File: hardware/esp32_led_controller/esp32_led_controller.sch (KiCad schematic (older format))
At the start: 47 parts, among them J1 USB_B, J2 CONN_01X09, J3 CONN_01X08, J4 BARREL_JACK, J5 CONN_01X03, J6 USB_C_Receptacle_USB2.0, Q1 Q_NPN_BEC, Q2 Q_NPN_BEC, SW1 SW_Push, U1 MCP1415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

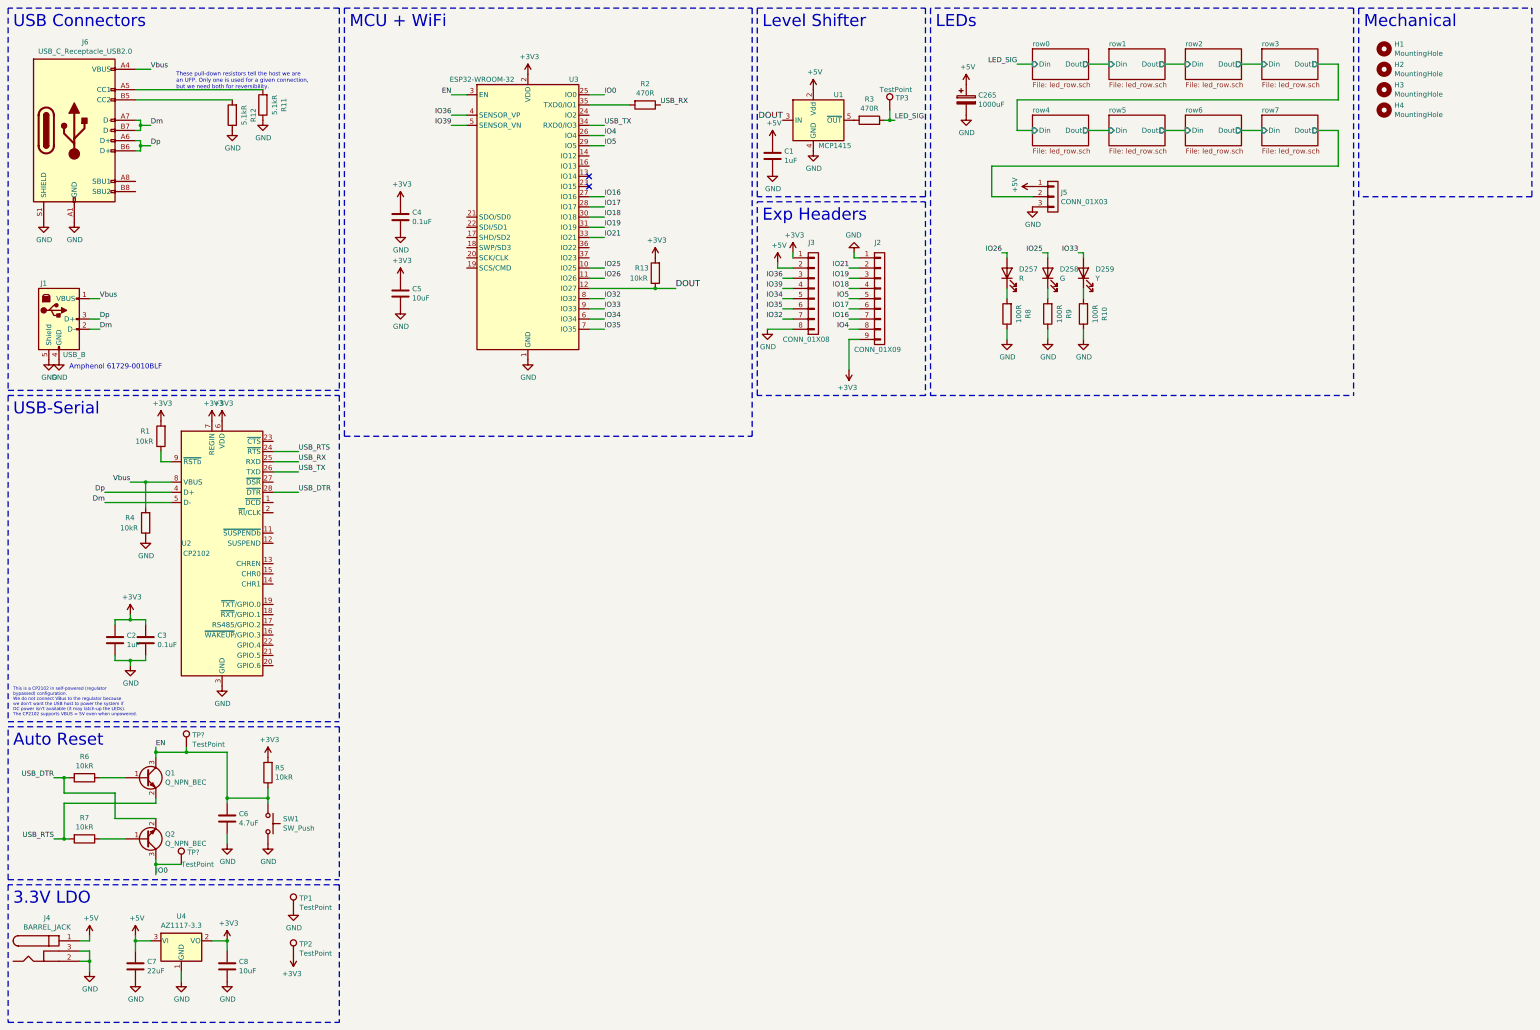
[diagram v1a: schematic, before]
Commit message: Added configuration jumpers
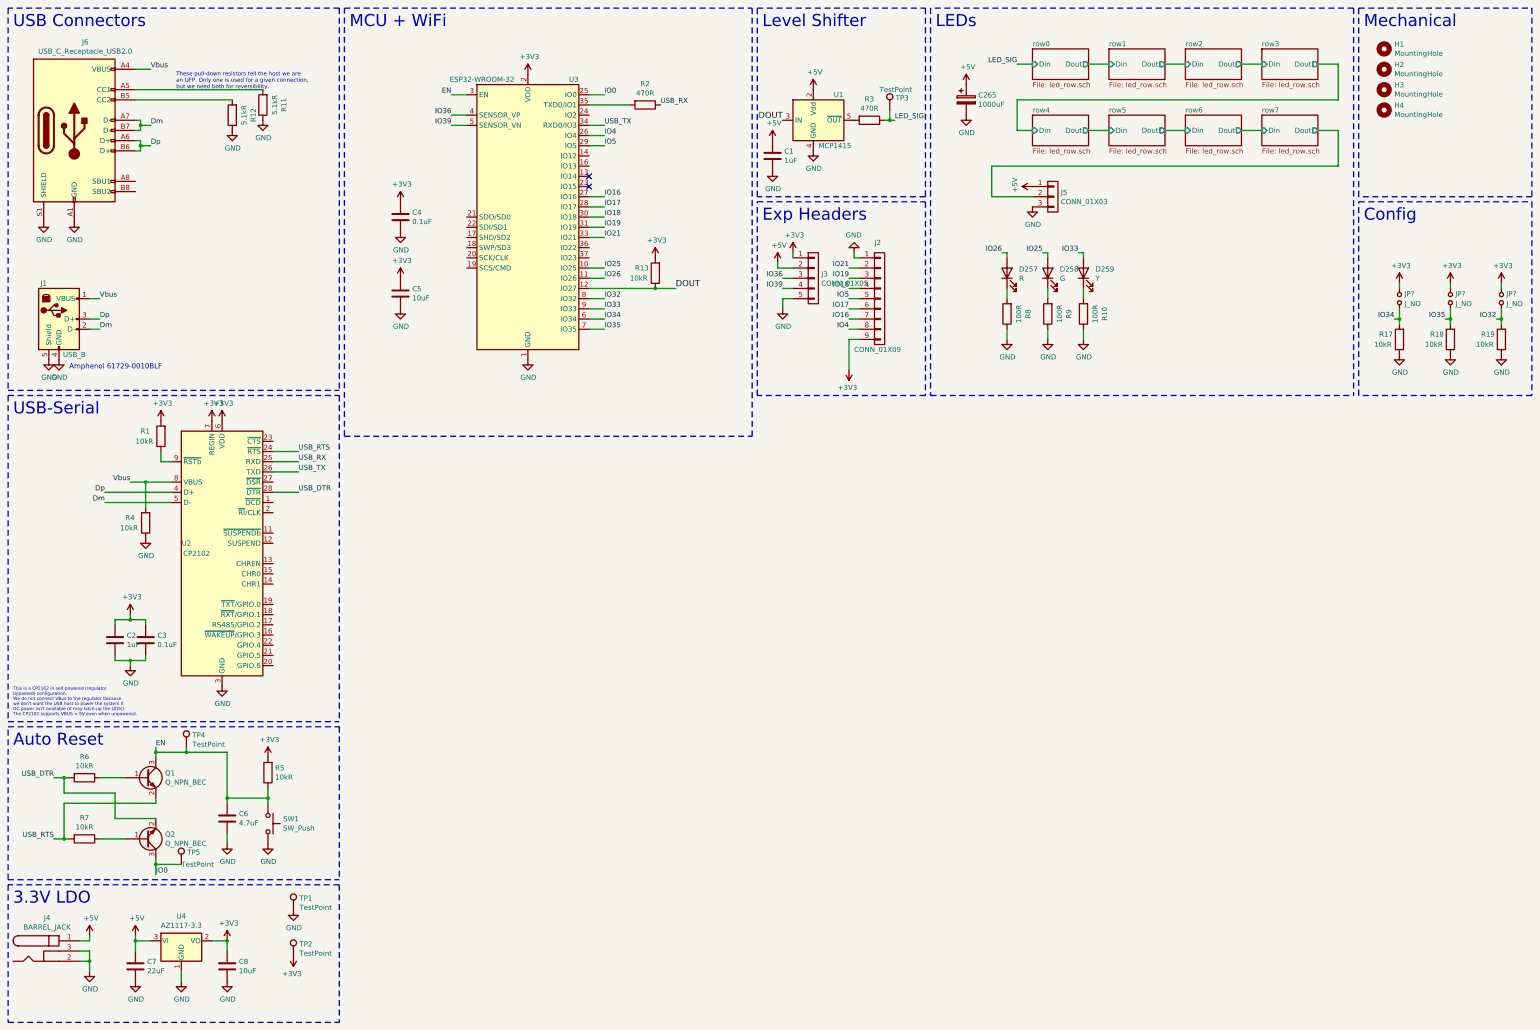
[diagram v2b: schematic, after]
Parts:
- removed J3: CONN_01X08, Connector_PinHeader_2.54mm:PinHeader_1x08_P2.54mm_Vertical, symbol conn:CONN_01X08
- added J3: CONN_01X05, Connector_PinHeader_2.54mm:PinHeader_1x05_P2.54mm_Vertical, symbol conn:CONN_01X05
- added JP? (x3): J_NO, Jumper:SolderJumper-2_P1.3mm_Open_TrianglePad1.0x1.5mm, symbol Device:Jumper_NO_Small
- added R17, R18, R19: 10kR, Resistor_SMD:R_0402_1005Metric, symbol Device:R
- gave numbers to parts that had none: 2
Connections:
- net +3V3: now also J3.1 (P1), JP?.1, JP?.1, JP?.1
- net +5V: now also J3.2 (P2)
- net GND: now also J3.5 (P5), R17.1, R18.1, R19.1
- net IO32: now also JP?.2, R19.2
- net IO34: now also JP?.2, R17.2
- net IO35: now also JP?.2, R18.2
- net IO36: now also J3.3 (P3)
- net IO39: now also J3.4 (P4)
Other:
- note added: "Config"
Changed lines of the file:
@@
 Wire Wire Line
 	6550 4100 6700 4100
-Text Label 8450 3800 2    50   ~ 0
+Text Label 14450 4000 2    50   ~ 0
 IO34
-Text Label 8450 3900 2    50   ~ 0
-IO35
 Text Label 6700 3900 0    50   ~ 0
 IO33
@@
 Wire Wire Line
 	6550 3900 6700 3900
-Text Label 8450 4000 2    50   ~ 0
-IO32
 Text Label 11350 3350 2    50   ~ 0
 IO33
@@
 	1    0    0    -1
 $EndComp
-Wire Wire Line
-	8450 4000 8550 4000
-Wire Wire Line
-	8550 3900 8450 3900
-Wire Wire Line
-	8550 3800 8450 3800
 Wire Wire Line
 	8450 3700 8550 3700
@@
 L power:GND #PWR?
 U 1 1 605F1340
-P 8300 4100
+P 8450 3900
 AR Path="/5F1ED570/605F1340" Ref="#PWR?"  Part="1"
 AR Path="/605F1340" Ref="#PWR01060"  Part="1"
-F 0 "#PWR01060" H 8300 3850 50  0001 C CNN
-F 1 "GND" H 8305 3927 50  0000 C CNN
-F 2 "" H 8300 4100 50  0001 C CNN
-F 3 "" H 8300 4100 50  0001 C CNN
-	1    8300 4100
+F 0 "#PWR01060" H 8450 3650 50  0001 C CNN
+F 1 "GND" H 8455 3727 50  0000 C CNN
+F 2 "" H 8450 3900 50  0001 C CNN
+F 3 "" H 8450 3900 50  0001 C CNN
+	1    8450 3900
 	1    0    0    -1
 $EndComp
@@
 Wire Wire Line
 	8400 3500 8550 3500
-Wire Wire Line
-	8300 4100 8550 4100
-$Comp
-L conn:CONN_01X08 J3
-U 1 1 606C16D0
-P 8750 3750
-F 0 "J3" H 8700 4250 50  0000 L CNN
-F 1 "CONN_01X08" H 8450 3300 50  0000 L CNN
-F 2 "Connector_PinHeader_2.54mm:PinHeader_1x08_P2.54mm_Vertical" H 8750 3750 50  0001 C CNN
-F 3 "" H 8750 3750 50  0001 C CNN
-	1    8750 3750
-	1    0    0    -1
-$EndComp
 $Comp
 L Device:LED D257
@@
 $EndComp
 $Comp
-L Connector:TestPoint TP?
+L Connector:TestPoint TP4
 U 1 1 6025CD38
 P 2600 8200
-F 0 "TP?" H 2658 8318 50  0000 L CNN
+F 0 "TP4" H 2658 8318 50  0000 L CNN
 F 1 "TestPoint" H 2658 8227 50  0000 L CNN
 F 2 "TestPoint:TestPoint_Loop_D3.50mm_Drill1.4mm_Beaded" H 2800 8200 50  0001 C CNN
@@
 $EndComp
 $Comp
-L Connector:TestPoint TP?
+L Connector:TestPoint TP5
 U 1 1 6025DADF
 P 2550 9350
-F 0 "TP?" H 2608 9468 50  0000 L CNN
+F 0 "TP5" H 2608 9468 50  0000 L CNN
 F 1 "TestPoint" H 2550 9350 50  0000 L CNN
 F 2 "TestPoint:TestPoint_Loop_D3.50mm_Drill1.4mm_Beaded" H 2750 9350 50  0001 C CNN
@@
 Wire Wire Line
 	2600 8250 3000 8250
+Wire Notes Line
+	14100 2850 15800 2850
+Wire Notes Line
+	15800 2850 15800 4750
+Wire Notes Line
+	15800 4750 14100 4750
+Wire Notes Line
+	14100 4750 14100 2850
+Text Notes 14150 3050 0    118  ~ 0
+Config
+$Comp
+L Device:R R?
+U 1 1 6028F8B2
+P 14500 4200
+AR Path="/5F1ED570/6028F8B2" Ref="R?"  Part="1"
+AR Path="/6028F8B2" Ref="R17"  Part="1"
+F 0 "R17" H 14700 4150 50  0000 R CNN
+F 1 "10kR" H 14750 4250 50  0000 R CNN
+F 2 "Resistor_SMD:R_0402_1005Metric" V 14430 4200 50  0001 C CNN
+F 3 "~" H 14500 4200 50  0001 C CNN
+F 4 "C25744" V 14500 4200 50  0001 C CNN "LCSC"
+	1    14500 4200
+	-1   0    0    1
+$EndComp
+$Comp
+L Device:R R?
+U 1 1 60290F37
+P 15000 4200
+AR Path="/5F1ED570/60290F37" Ref="R?"  Part="1"
+AR Path="/60290F37" Ref="R18"  Part="1"
+F 0 "R18" H 15200 4150 50  0000 R CNN
+F 1 "10kR" H 15250 4250 50  0000 R CNN
+F 2 "Resistor_SMD:R_0402_1005Metric" V 14930 4200 50  0001 C CNN
+F 3 "~" H 15000 4200 50  0001 C CNN
+F 4 "C25744" V 15000 4200 50  0001 C CNN "LCSC"
+	1    15000 4200
+	-1   0    0    1
+$EndComp
+$Comp
+L Device:R R?
+U 1 1 6029126C
+P 15500 4200
+AR Path="/5F1ED570/6029126C" Ref="R?"  Part="1"
+AR Path="/6029126C" Ref="R19"  Part="1"
+F 0 "R19" H 15700 4150 50  0000 R CNN
+F 1 "10kR" H 15750 4250 50  0000 R CNN
+F 2 "Resistor_SMD:R_0402_1005Metric" V 15430 4200 50  0001 C CNN
+F 3 "~" H 15500 4200 50  0001 C CNN
+F 4 "C25744" V 15500 4200 50  0001 C CNN "LCSC"
+	1    15500 4200
+	-1   0    0    1
+$EndComp
+$Comp
+L power:+3V3 #PWR?
+U 1 1 6029175F
+P 14500 3650
+AR Path="/5F1ED570/6029175F" Ref="#PWR?"  Part="1"
+AR Path="/6029175F" Ref="#PWR01074"  Part="1"
+F 0 "#PWR01074" H 14500 3500 50  0001 C CNN
+F 1 "+3V3" H 14515 3823 50  0000 C CNN
+F 2 "" H 14500 3650 50  0001 C CNN
+F 3 "" H 14500 3650 50  0001 C CNN
+	1    14500 3650
+	1    0    0    -1
+$EndComp
+$Comp
+L power:+3V3 #PWR?
+U 1 1 60291FEB
+P 15000 3650
+AR Path="/5F1ED570/60291FEB" Ref="#PWR?"  Part="1"
+AR Path="/60291FEB" Ref="#PWR01075"  Part="1"
+F 0 "#PWR01075" H 15000 3500 50  0001 C CNN
+F 1 "+3V3" H 15015 3823 50  0000 C CNN
+F 2 "" H 15000 3650 50  0001 C CNN
+F 3 "" H 15000 3650 50  0001 C CNN
+	1    15000 3650
+	1    0    0    -1
+$EndComp
+$Comp
+L power:+3V3 #PWR?
+U 1 1 6029236B
+P 15500 3650
+AR Path="/5F1ED570/6029236B" Ref="#PWR?"  Part="1"
+AR Path="/6029236B" Ref="#PWR01076"  Part="1"
+F 0 "#PWR01076" H 15500 3500 50  0001 C CNN
+F 1 "+3V3" H 15515 3823 50  0000 C CNN
+F 2 "" H 15500 3650 50  0001 C CNN
+F 3 "" H 15500 3650 50  0001 C CNN
+	1    15500 3650
+	1    0    0    -1
+$EndComp
+$Comp
+L power:GND #PWR?
+U 1 1 60299D69
+P 14500 4350
+AR Path="/5F1ED570/60299D69" Ref="#PWR?"  Part="1"
+AR Path="/60299D69" Ref="#PWR01077"  Part="1"
+F 0 "#PWR01077" H 14500 4100 50  0001 C CNN
+F 1 "GND" H 14505 4177 50  0000 C CNN
+F 2 "" H 14500 4350 50  0001 C CNN
+F 3 "" H 14500 4350 50  0001 C CNN
+	1    14500 4350
+	1    0    0    -1
+$EndComp
+$Comp
+L power:GND #PWR?
+U 1 1 6029A13A
+P 15000 4350
+AR Path="/5F1ED570/6029A13A" Ref="#PWR?"  Part="1"
+AR Path="/6029A13A" Ref="#PWR01078"  Part="1"
+F 0 "#PWR01078" H 15000 4100 50  0001 C CNN
+F 1 "GND" H 15005 4177 50  0000 C CNN
+F 2 "" H 15000 4350 50  0001 C CNN
+F 3 "" H 15000 4350 50  0001 C CNN
+	1    15000 4350
+	1    0    0    -1
+$EndComp
+$Comp
+L power:GND #PWR?
+U 1 1 6029A31F
+P 15500 4350
+AR Path="/5F1ED570/6029A31F" Ref="#PWR?"  Part="1"
+AR Path="/6029A31F" Ref="#PWR01079"  Part="1"
+F 0 "#PWR01079" H 15500 4100 50  0001 C CNN
+F 1 "GND" H 15505 4177 50  0000 C CNN
+F 2 "" H 15500 4350 50  0001 C CNN
+F 3 "" H 15500 4350 50  0001 C CNN
+	1    15500 4350
+	1    0    0    -1
+$EndComp
+Wire Wire Line
+	14450 4000 14500 4000
+Wire Wire Line
+	14500 4000 14500 4050
+Connection ~ 14500 4000
+Text Label 14950 4000 2    50   ~ 0
+IO35
+Text Label 15450 4000 2    50   ~ 0
+IO32
+$Comp
+L conn:CONN_01X05 J3
+U 1 1 602A9206
+P 8750 3600
+F 0 "J3" H 8828 3641 50  0000 L CNN
+F 1 "CONN_01X05" H 8828 3550 50  0000 L CNN
+F 2 "Connector_PinHeader_2.54mm:PinHeader_1x05_P2.54mm_Vertical" H 8750 3600 50  0001 C CNN
+F 3 "" H 8750 3600 50  0001 C CNN
+	1    8750 3600
+	1    0    0    -1
+$EndComp
+Wire Wire Line
+	8450 3900 8450 3800
+Wire Wire Line
+	8450 3800 8550 3800
+Wire Wire Line
+	14950 4000 15000 4000
+Connection ~ 15000 4000
+Wire Wire Line
+	15000 4000 15000 4050
+Wire Wire Line
+	15450 4000 15500 4000
+Connection ~ 15500 4000
+Wire Wire Line
+	15500 4000 15500 4050
+$Comp
+L Device:Jumper_NO_Small JP?
+U 1 1 60328712
+P 15000 3800
+F 0 "JP?" V 14954 3848 50  0000 L CNN
+F 1 "J_NO" V 15050 3850 50  0000 L CNN
+F 2 "Jumper:SolderJumper-2_P1.3mm_Open_TrianglePad1.0x1.5mm" H 15000 3800 50  0001 C CNN
+F 3 "~" H 15000 3800 50  0001 C CNN
+	1    15000 3800
+	0    1    1    0
+$EndComp
+$Comp
+L Device:Jumper_NO_Small JP?
+U 1 1 60329C4C
+P 14500 3800
+F 0 "JP?" V 14454 3848 50  0000 L CNN
+F 1 "J_NO" V 14550 3850 50  0000 L CNN
+F 2 "Jumper:SolderJumper-2_P1.3mm_Open_TrianglePad1.0x1.5mm" H 14500 3800 50  0001 C CNN
+F 3 "~" H 14500 3800 50  0001 C CNN
+	1    14500 3800
+	0    1    1    0
+$EndComp
+$Comp
+L Device:Jumper_NO_Small JP?
+U 1 1 6032A0A5
+P 15500 3800
+F 0 "JP?" V 15454 3848 50  0000 L CNN
+F 1 "J_NO" V 15550 3850 50  0000 L CNN
+F 2 "Jumper:SolderJumper-2_P1.3mm_Open_TrianglePad1.0x1.5mm" H 15500 3800 50  0001 C CNN
+F 3 "~" H 15500 3800 50  0001 C CNN
+	1    15500 3800
+	0    1    1    0
+$EndComp
+Wire Wire Line
+	15500 3650 15500 3700
+Wire Wire Line
+	15500 3900 15500 4000
+Wire Wire Line
+	15000 3900 15000 4000
+Wire Wire Line
+	15000 3650 15000 3700
+Wire Wire Line
+	14500 3900 14500 4000
+Wire Wire Line
+	14500 3650 14500 3700
 $EndSCHEMATC

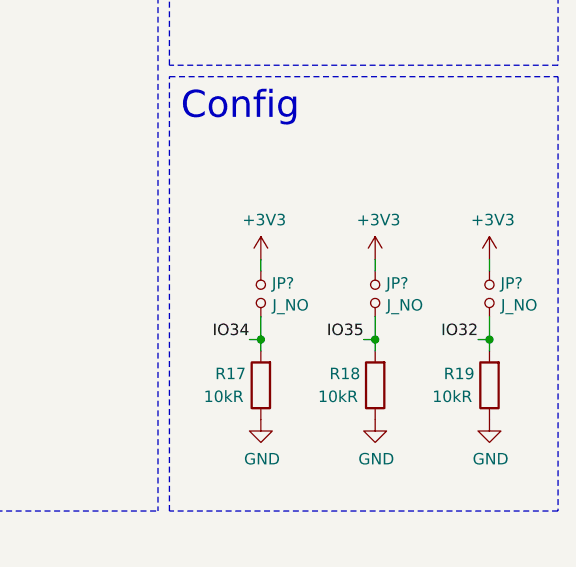
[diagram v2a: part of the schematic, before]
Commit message: Added missing annotations
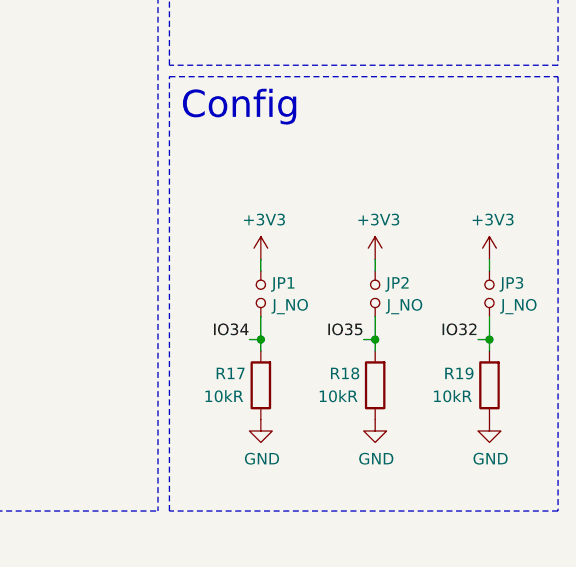
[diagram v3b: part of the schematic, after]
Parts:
- gave numbers to parts that had none: 3
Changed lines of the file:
@@
 	15500 4000 15500 4050
 $Comp
-L Device:Jumper_NO_Small JP?
+L Device:Jumper_NO_Small JP2
 U 1 1 60328712
 P 15000 3800
-F 0 "JP?" V 14954 3848 50  0000 L CNN
+F 0 "JP2" V 14954 3848 50  0000 L CNN
 F 1 "J_NO" V 15050 3850 50  0000 L CNN
 F 2 "Jumper:SolderJumper-2_P1.3mm_Open_TrianglePad1.0x1.5mm" H 15000 3800 50  0001 C CNN
@@
 $EndComp
 $Comp
-L Device:Jumper_NO_Small JP?
+L Device:Jumper_NO_Small JP1
 U 1 1 60329C4C
 P 14500 3800
-F 0 "JP?" V 14454 3848 50  0000 L CNN
+F 0 "JP1" V 14454 3848 50  0000 L CNN
 F 1 "J_NO" V 14550 3850 50  0000 L CNN
 F 2 "Jumper:SolderJumper-2_P1.3mm_Open_TrianglePad1.0x1.5mm" H 14500 3800 50  0001 C CNN
@@
 $EndComp
 $Comp
-L Device:Jumper_NO_Small JP?
+L Device:Jumper_NO_Small JP3
 U 1 1 6032A0A5
 P 15500 3800
-F 0 "JP?" V 15454 3848 50  0000 L CNN
+F 0 "JP3" V 15454 3848 50  0000 L CNN
 F 1 "J_NO" V 15550 3850 50  0000 L CNN
 F 2 "Jumper:SolderJumper-2_P1.3mm_Open_TrianglePad1.0x1.5mm" H 15500 3800 50  0001 C CNN

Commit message: Added rev4 hardware design
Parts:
- removed C1: 1uF, Capacitor_SMD:C_0402_1005Metric, symbol Device:C
- removed C265: 1000uF, Capacitor_SMD:CP_Elec_10x10, symbol Device:CP
- removed D257: R, LED_SMD:LED_0603_1608Metric, symbol Device:LED
- removed H3: MountingHole, MountingHole:MountingHole_2.2mm_M2, symbol Mechanical:MountingHole
- removed J1: USB_B, Amphenol:Amphenol_61729_0010BLF, symbol esp32_led_controller-rescue:USB_B-Connector
- removed J3: CONN_01X05, Connector_PinHeader_2.54mm:PinHeader_1x05_P2.54mm_Vertical, symbol conn:CONN_01X05
- removed J4: BARREL_JACK, dc_jack:DC-005C-25A, symbol conn:BARREL_JACK
- removed JP3: J_NO, Jumper:SolderJumper-2_P1.3mm_Open_TrianglePad1.0x1.5mm, symbol Device:Jumper_NO_Small
- removed R4: 10kR, Resistor_SMD:R_0402_1005Metric, symbol Device:R
- removed R8: 100R, Resistor_SMD:R_0402_1005Metric, symbol Device:R
- removed TP3, TP4, TP5: TestPoint, TestPoint:TestPoint_Loop_D3.50mm_Drill1.4mm_Beaded, symbol Connector:TestPoint
- removed U1: MCP1415, Package_TO_SOT_SMD:SOT-23-5, symbol Driver_FET:MCP1415
- removed U2: CP2102, Package_DFN_QFN:QFN-28-1EP_5x5mm_P0.5mm_EP3.35x3.35mm, symbol Interface_USB:CP2102N-A01-GQFN28
- added C1: 470uF, Capacitor_THT:CP_Radial_D5.0mm_P2.00mm, symbol Device:CP
- added C13, C9: 0.1uF, Capacitor_SMD:C_0402_1005Metric, symbol Device:C
- added TP6: TestPoint, TestPoint:TestPoint_Pad_4.0x4.0mm, symbol Connector:TestPoint
- added U1: SN74LV1T08, Package_TO_SOT_SMD:SOT-353_SC-70-5, symbol 74xGxx:74AHC1G08
- added U2: CH340B/CH340C, Package_SO:SOIC-16_3.9x9.9mm_P1.27mm, symbol Interface_USB:CH340C
- added U5: AP2172A, Package_SO:SO-8_3.9x4.9mm_P1.27mm, symbol ap2172:AP2172
- C2: value 1uF -> 0.1uF; LCSC C52923 -> C1525
- C7: value 22uF -> 10uF; footprint Capacitor_SMD:C_0805_2012Metric -> Capacitor_SMD:C_0402_1005Metric; LCSC C45783 -> C15525
- J5: footprint Connector_PinHeader_2.54mm:PinHeader_1x03_P2.54mm_Vertical -> terminal_block:KF128L-3.81-3P; LCSC (none) -> C474933
- TP1, TP2: footprint TestPoint:TestPoint_Loop_D3.50mm_Drill1.4mm_Beaded -> TestPoint:TestPoint_Pad_4.0x4.0mm
- U4: footprint Package_TO_SOT_SMD:SOT-223-3_TabPin2 -> Package_TO_SOT_SMD:SOT-89-3; LCSC C92102 -> C108493
- renumbered H4 to H3
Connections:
- net IO36 is gone; now on net CC1: U3.4 (SENSOR_VP)
- net IO39 is gone; now on net CC2: U3.5 (SENSOR_VN)
- net Vbus is gone; now on net +5V: J6.A4 (VBUS), J6.A9 (VBUS), J6.B4 (VBUS), J6.B9 (VBUS)
- net +3V3: no longer C2.1, C3.1, R1.2, R13.2, TP2.1
- net +5V: now also C2.1, C13.1, C9.1, U1.5 (VCC), U2.16 (VCC), U5.2 (IN); no longer J5.1 (P1)
- net DOUT: now also R13.2, U1.1; no longer R13.1
- net Dm: now also U2.6 (UD-)
- net Dp: now also U2.5 (UD+)
- net GND: now also R1.1, R13.1, C1.2, C13.2, C9.2, U1.3 (GND), U2.1 (GND), U5.1 (GND); no longer TP1.1
- net IO32: now also D259.2 (A); no longer R19.2
- net IO33: now also D258.2 (A); no longer D259.2 (A)
- net IO4: now also TP6.1; no longer J2.8 (P8)
- net LED_SIG: now also R3.2, U1.4; no longer R3.1
- net USB_DTR: now also U2.13 (~DTR)
- net USB_RTS: now also U2.14 (~RTS)
- net USB_RX: now also U2.3 (RXD)
- net USB_TX: now also U2.2 (TXD)
- net LED_ON0: now reaches U3.14 (IO12)
- net LED_ON0: now also R19.2, U1.2, U5.3 (EN1)
- net IO15: now reaches U3.23 (IO15)
- net IO15: now also J2.8 (P8), TP1.1
- net IO2: now reaches U3.24 (IO2)
- net IO2: now also TP2.1
- net CC1: now reaches J6.A5 (CC1), R11.2
- net CC2: now reaches J6.B5 (CC2), R12.2
- net IO25: no longer names the net of U3.10 (IO25)
- net IO25: no longer D258.2 (A)
- net IO26 renamed LED_ON1
- net LED_ON1: now also R1.2, U5.4 (EN2)
- net row7/Dout: no longer names the net of J5.2 (P2)
- net row7/Dout: now also R3.1
- new net: C3.1, U2.4 (V3)
- new net LED_5V: C1.1, J5.1 (P1), U5.6 (OUT2), U5.7 (OUT1)
- no-connect marks 2 -> 1
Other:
- note removed: "Amphenol 61729-0010BLF"
- note removed: "Level Shifter"
- note removed: "This is a CP2102 in self-powered (regulator\nbypassed) configuration.\nWe do not connect VBus to the regulator because\nwe don't want the USB host to power the system if\nDC power isn't available (it may latch-up the LEDs).\nThe CP2102 supports VBUS = 5V even when unpowered."
- moved on the sheet: C6, C7, C8, D258, D259, H1, H2, H3, J2, J5, JP1, JP2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
